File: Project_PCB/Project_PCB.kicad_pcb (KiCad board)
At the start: 2 copper layers, 70.6 x 70.6 mm, 51 parts, among them J1 USB_C_2.0, J2 Myoware Connector, J3 Conn_01x02, SW1 RESET, SW2 BOOT, SW3 POWER, U1 ESP32-S3-WROOM-1, U2 RT9080-33GJ5, U3 MCP73831T-2ACI/OT, U4 LMV321

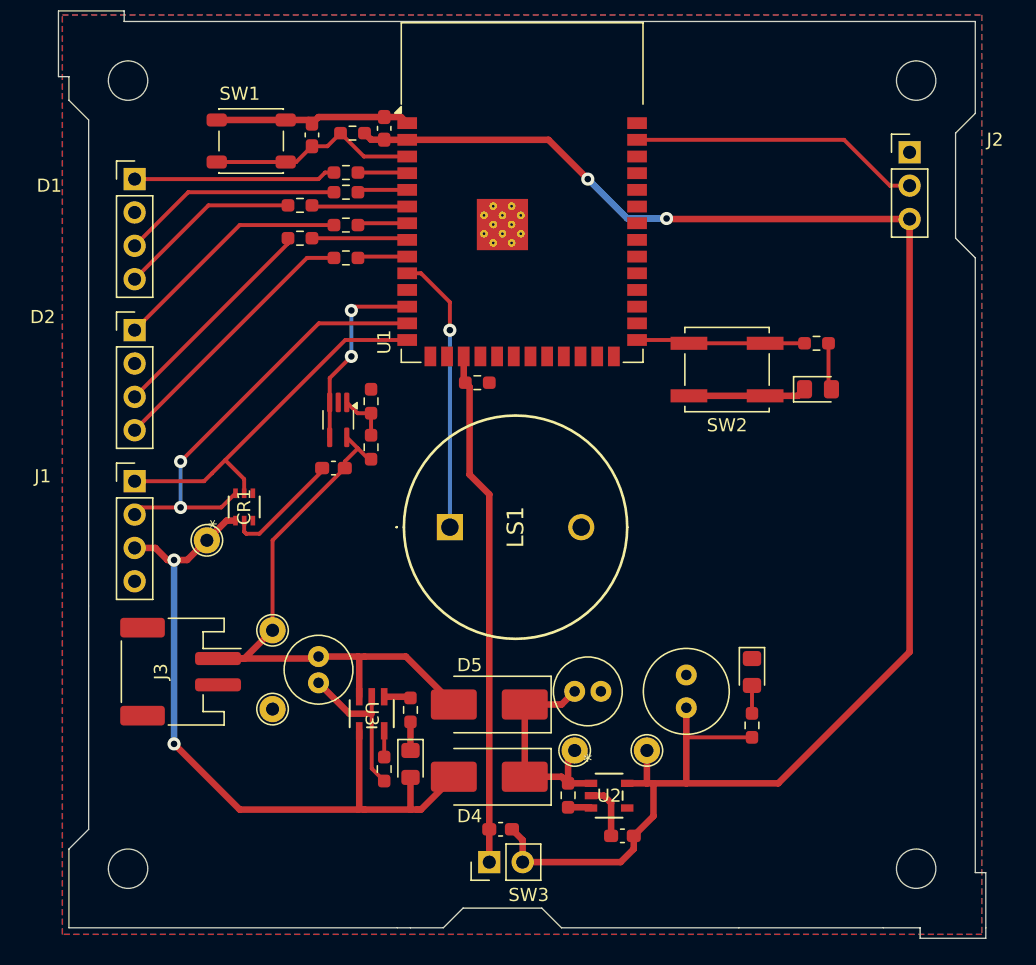
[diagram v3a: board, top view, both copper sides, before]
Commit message: Updated PCB layout to fix issues with design
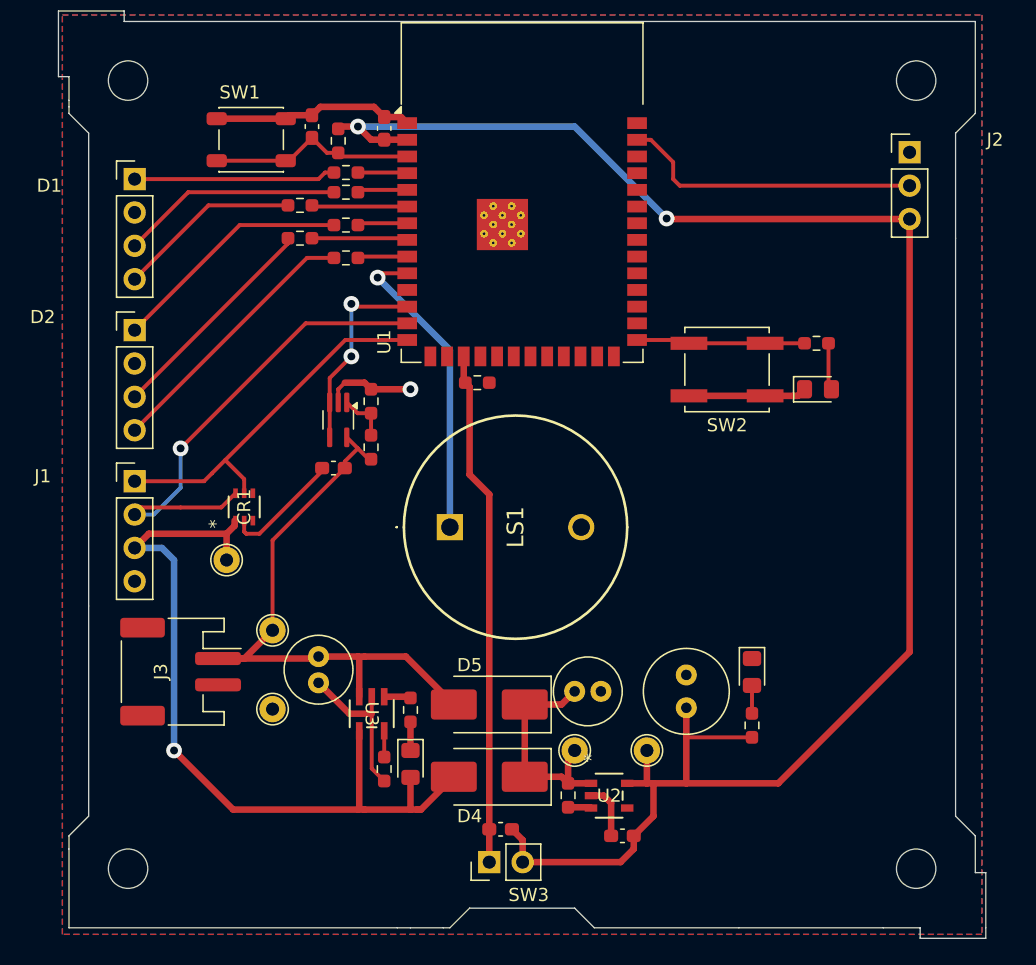
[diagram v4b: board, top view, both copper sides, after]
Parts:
- moved TP4 2.12 mm to (12.0, 41.0)
- moved R1 1.24 mm to (20.5, 9.09), turned to -90 degrees
- moved C1 0.64 mm to (18.5, 8.00)
- moved SW1 0.10 mm to (13.9, 9.00)
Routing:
- net GND: track 49.2 -> 56.5 mm, vias 0 -> 1
- net +3V3: track 133.4 -> 139.8 mm
- net VBUS: track 56.1 -> 61.3 mm, vias 2 -> 1
- net ESP19/D-: track 33.5 -> 36.9 mm, vias 2 -> 1
- net Net-(U1-IO17): track 21.3 -> 23.7 mm
- net Net-(J2-Pin_2): track 22.2 -> 23.0 mm
- net ESP~{RST}: track 16.1 -> 15.4 mm
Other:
- outline, holes or cut-outs redrawn
